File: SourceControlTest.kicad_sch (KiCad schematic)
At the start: 4 parts

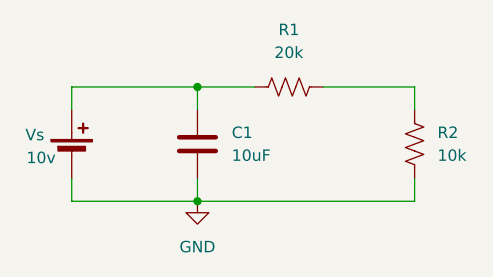
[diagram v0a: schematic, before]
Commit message: deleted capacitor
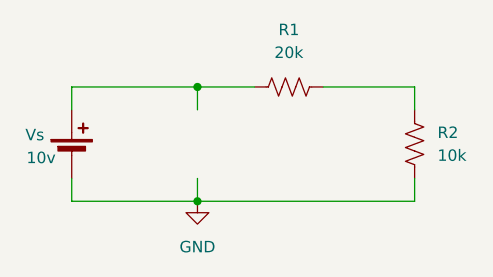
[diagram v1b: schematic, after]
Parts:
- removed C1: 10uF, symbol Device:C
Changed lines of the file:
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@@
-	)
-	(symbol
-		(lib_id "Device:C")
-		(at 128.27 95.25 0)
-		(unit 1)
-		(body_style 1)
-		(exclude_from_sim no)
-		(in_bom yes)
-		(on_board yes)
-		(in_pos_files yes)
-		(dnp no)
-		(fields_autoplaced yes)
-		(property "Reference" "C1"
-			(at 132.08 93.9799 0)
-			(show_name no)
-			(do_not_autoplace no)
-			(effects
-				(font
-					(size 1.27 1.27)
-				)
-				(justify left)
-			)
-		)
-		(property "Value" "10uF"
-			(at 132.08 96.5199 0)
-			(show_name no)
-			(do_not_autoplace no)
-			(effects
-				(font
-					(size 1.27 1.27)
-				)
-				(justify left)
-			)
-		)
-		(property "Footprint" ""
-			(at 129.2352 99.06 0)
-			(hide yes)
-			(show_name no)
-			(do_not_autoplace no)
-			(effects
-				(font
-					(size 1.27 1.27)
-				)
-			)
-		)
-		(property "Datasheet" ""
-			(at 128.27 95.25 0)
-			(hide yes)
-			(show_name no)
-			(do_not_autoplace no)
-			(effects
-				(font
-					(size 1.27 1.27)
-				)
-			)
-		)
-		(property "Description" "Unpolarized capacitor"
-			(at 128.27 95.25 0)
-			(hide yes)
-			(show_name no)
-			(do_not_autoplace no)
-			(effects
-				(font
-					(size 1.27 1.27)
-				)
-			)
-		)
-		(pin "2"
-		)
-		(pin "1"
-		)
-		(instances
-			(project "SourceControlTest"
-				(path "/5d981c2c-ab3d-4850-ba6d-abf03e2cd683"
-					(reference "C1")
-					(unit 1)
-				)
-			)
-		)
 	)
 	(symbol

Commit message: Revert "deleted capacitor"
This reverts commit d5b02636a01619e9b602a21c2b5c62289a5c960a.
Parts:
- added C1: 10uF, symbol Device:C
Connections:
- net GND: now also C1.2
- net at R1.1, Vs.1 (+): now also C1.1
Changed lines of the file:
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@@
+	)
+	(symbol
+		(lib_id "Device:C")
+		(at 128.27 95.25 0)
+		(unit 1)
+		(body_style 1)
+		(exclude_from_sim no)
+		(in_bom yes)
+		(on_board yes)
+		(in_pos_files yes)
+		(dnp no)
+		(fields_autoplaced yes)
+		(property "Reference" "C1"
+			(at 132.08 93.9799 0)
+			(show_name no)
+			(do_not_autoplace no)
+			(effects
+				(font
+					(size 1.27 1.27)
+				)
+				(justify left)
+			)
+		)
+		(property "Value" "10uF"
+			(at 132.08 96.5199 0)
+			(show_name no)
+			(do_not_autoplace no)
+			(effects
+				(font
+					(size 1.27 1.27)
+				)
+				(justify left)
+			)
+		)
+		(property "Footprint" ""
+			(at 129.2352 99.06 0)
+			(hide yes)
+			(show_name no)
+			(do_not_autoplace no)
+			(effects
+				(font
+					(size 1.27 1.27)
+				)
+			)
+		)
+		(property "Datasheet" ""
+			(at 128.27 95.25 0)
+			(hide yes)
+			(show_name no)
+			(do_not_autoplace no)
+			(effects
+				(font
+					(size 1.27 1.27)
+				)
+			)
+		)
+		(property "Description" "Unpolarized capacitor"
+			(at 128.27 95.25 0)
+			(hide yes)
+			(show_name no)
+			(do_not_autoplace no)
+			(effects
+				(font
+					(size 1.27 1.27)
+				)
+			)
+		)
+		(pin "2"
+		)
+		(pin "1"
+		)
+		(instances
+			(project "SourceControlTest"
+				(path "/5d981c2c-ab3d-4850-ba6d-abf03e2cd683"
+					(reference "C1")
+					(unit 1)
+				)
+			)
+		)
 	)
 	(symbol
